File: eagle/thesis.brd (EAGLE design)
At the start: 99.1 x 60.2 mm, 14 parts

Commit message: routed thesis board
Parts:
- moved U$4 46.0 mm to (28.3, 51.9), turned to 180 degrees
- moved U$2 11.0 mm to (22.1, 1.65), turned to 90 degrees
- moved U$3 0.89 mm to (-2.67, 14.7)
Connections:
- new net D52: U$1.52
- new net D53: U$1.53
- net ACCELCS: now also U$1.8; no longer U$1.53
- net GND: no longer U$1.GND_DEBUG
- net RX3H: now also U$2.P$11
- net SDCS: now also U$1.9; no longer U$1.52
- net TX3H: no longer U$2.P$11
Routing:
- net MOSI: track 0.00 -> 189.0 mm, vias 0 -> 6
- net SCLK: track 0.00 -> 124.6 mm, vias 0 -> 5
- net RX3H: track 0.00 -> 96.6 mm
- net 3V3: track 107.0 -> 197.4 mm
- net MISO: track 0.00 -> 73.8 mm, vias 0 -> 4
- net GND: track 244.3 -> 280.4 mm, vias 0 -> 1
- net SDCS: track 0.00 -> 34.4 mm, vias 0 -> 3
- net RX3: track 83.4 -> 105.2 mm, vias 2 -> 0
- net TX3H: track 77.4 -> 97.8 mm
- net ACCELCS: track 0.00 -> 15.2 mm
- net 5V: track 132.2 -> 146.2 mm, vias 0 -> 1
- net TX3: track 73.7 -> 86.5 mm
- net TX2H: track 35.5 -> 25.7 mm
- net SDA2: track 82.6 -> 88.6 mm
- net RX2: track 97.2 -> 102.6 mm
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
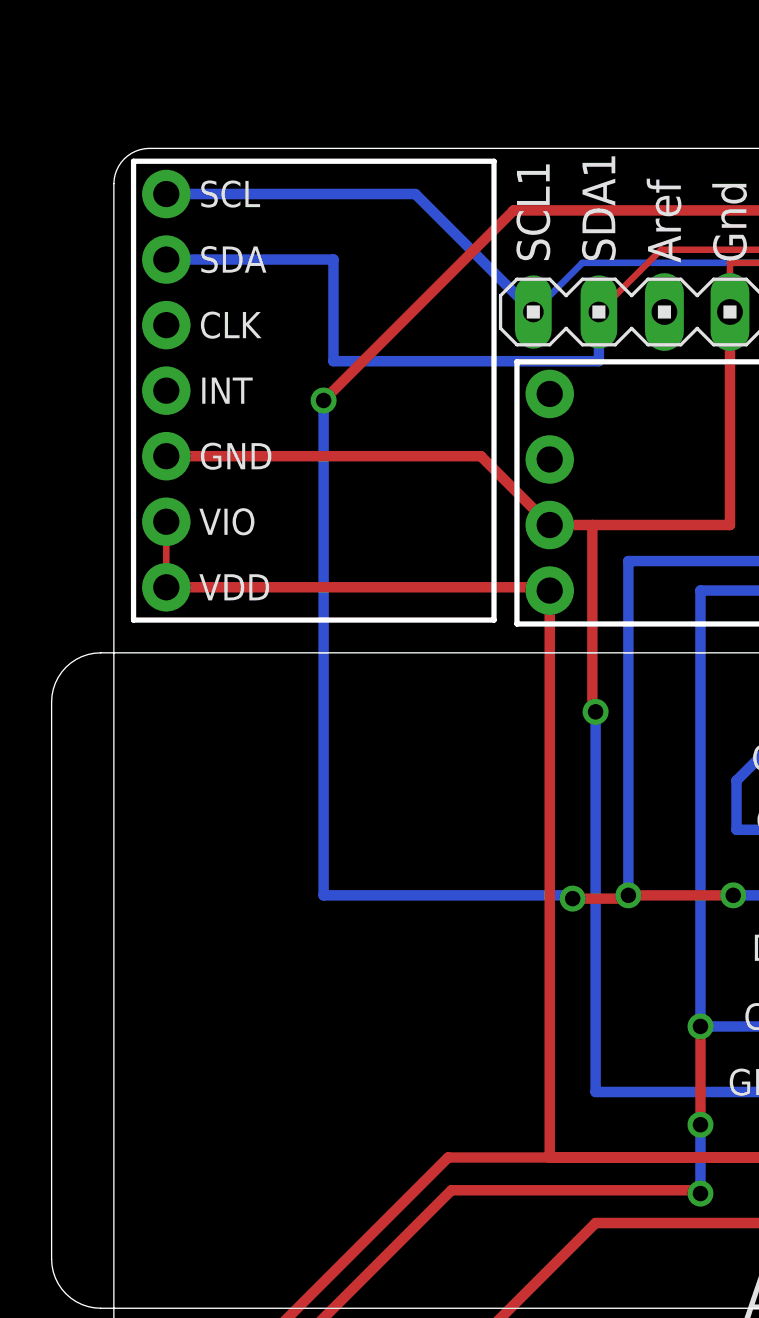
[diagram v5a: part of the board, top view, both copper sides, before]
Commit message: flipped itg3200 board
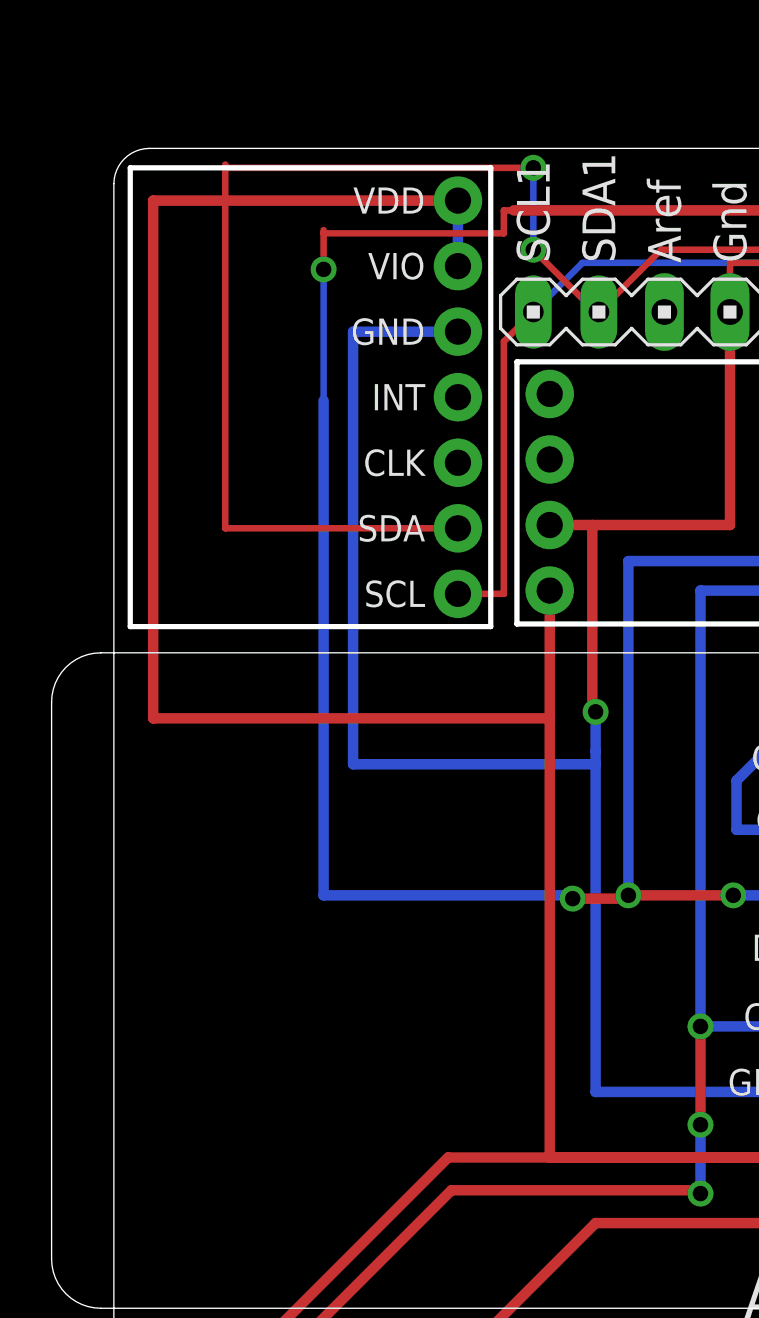
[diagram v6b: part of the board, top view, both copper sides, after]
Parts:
- moved U$7 22.5 mm to (0.64, 59.4), turned to 270 degrees
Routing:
- net 3V3: track 197.4 -> 229.8 mm
- net SDA2: track 88.6 -> 107.8 mm, vias 0 -> 2
- net GND: track 280.4 -> 294.7 mm
- net MOSI: track 189.0 -> 193.4 mm
- net SCL: track 85.0 -> 82.1 mm
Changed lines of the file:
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@@
 <element name="U$2" library="SparkFun-Boards" package="LOGIC_LEVEL_CONVERTER" value="LOGIC_LEVEL_CONVERTER" x="22.098" y="1.651" rot="R90"/>
 <element name="U$4" library="adxl362" package="ADXL362" value="ADXL362" x="28.321" y="51.943" rot="R180"/>
-<element name="U$7" library="ITG3200" package="ITG3200" value="ITG3200" x="14.732" y="41.91" rot="R90"/>
+<element name="U$7" library="ITG3200" package="ITG3200" value="ITG3200" x="0.635" y="59.436" rot="R270"/>
 <element name="U$3" library="MICROSD" package="MICROSD" value="MICROSD" x="-2.667" y="14.732"/>
 <element name="X1" library="con-subd" package="F09V" value="" x="81.407" y="36.449" rot="R90">
@@
 <contactref element="U$4" pad="VCC"/>
 <contactref element="U$2" pad="P$3"/>
-<wire x1="2.032" y1="45.72" x2="2.032" y2="43.18" width="0.254" layer="1"/>
 <wire x1="87.503" y1="9.398" x2="84.455" y2="9.398" width="0.254" layer="1"/>
 <wire x1="87.503" y1="3.683" x2="87.503" y2="9.398" width="0.254" layer="1"/>
@@
 <wire x1="34.671" y1="7.493" x2="43.434" y2="7.493" width="0.254" layer="16"/>
 <wire x1="32.766" y1="5.588" x2="34.671" y2="7.493" width="0.254" layer="16"/>
-<wire x1="2.032" y1="43.18" x2="16.891" y2="43.18" width="0.4064" layer="1"/>
-<wire x1="16.891" y1="43.18" x2="16.891" y2="43.053" width="0.4064" layer="1"/>
-<wire x1="16.891" y1="43.053" x2="16.891" y2="21.082" width="0.4064" layer="1"/>
+<wire x1="16.891" y1="43.053" x2="16.891" y2="38.1" width="0.4064" layer="1"/>
+<wire x1="16.891" y1="38.1" x2="16.891" y2="21.082" width="0.4064" layer="1"/>
 <wire x1="2.794" y1="10.922" x2="2.794" y2="0.889" width="0.4064" layer="1"/>
 <via x="2.794" y="0.889" extent="1-16" drill="0.6"/>
@@
 <wire x1="27.813" y1="21.082" x2="12.954" y2="21.082" width="0.4064" layer="1"/>
 <wire x1="12.954" y1="21.082" x2="2.794" y2="10.922" width="0.4064" layer="1"/>
+<wire x1="13.335" y1="55.626" x2="13.335" y2="58.166" width="0.4064" layer="16"/>
+<wire x1="16.891" y1="43.18" x2="16.891" y2="43.053" width="0.4064" layer="1"/>
+<wire x1="16.891" y1="38.1" x2="1.524" y2="38.1" width="0.4064" layer="1"/>
+<wire x1="1.524" y1="38.1" x2="1.524" y2="58.166" width="0.4064" layer="1"/>
+<wire x1="1.524" y1="58.166" x2="13.335" y2="58.166" width="0.4064" layer="1"/>
 </signal>
 <signal name="5V">
@@
 <wire x1="86.741" y1="50.038" x2="86.741" y2="57.785" width="0.4064" layer="1"/>
 <wire x1="86.741" y1="57.785" x2="15.494" y2="57.785" width="0.4064" layer="1"/>
-<wire x1="15.494" y1="57.785" x2="8.128" y2="50.419" width="0.4064" layer="1"/>
-<via x="8.128" y="50.419" extent="1-16" drill="0.6"/>
 <wire x1="8.128" y1="50.419" x2="8.128" y2="31.242" width="0.4064" layer="16"/>
 <wire x1="8.128" y1="31.242" x2="17.78" y2="31.242" width="0.4064" layer="16"/>
@@
 <wire x1="17.78" y1="31.115" x2="19.939" y2="31.115" width="0.4064" layer="1"/>
 <wire x1="19.939" y1="31.115" x2="19.939" y2="31.242" width="0.4064" layer="1"/>
+<wire x1="15.494" y1="57.785" x2="15.113" y2="57.785" width="0.254" layer="1"/>
+<wire x1="15.113" y1="57.785" x2="15.113" y2="56.896" width="0.254" layer="1"/>
+<wire x1="15.113" y1="56.896" x2="8.128" y2="56.896" width="0.254" layer="1"/>
+<wire x1="8.128" y1="56.896" x2="8.128" y2="57.023" width="0.254" layer="1"/>
+<wire x1="8.128" y1="50.419" x2="8.128" y2="55.499" width="0.254" layer="16"/>
+<via x="8.128" y="55.499" extent="1-16" drill="0.6"/>
+<wire x1="8.128" y1="55.499" x2="8.128" y2="56.896" width="0.254" layer="1"/>
 </signal>
 <signal name="RX2">
@@
 <wire x1="81.661" y1="55.753" x2="18.161" y2="55.753" width="0.254" layer="16"/>
 <wire x1="83.566" y1="53.848" x2="81.661" y2="55.753" width="0.254" layer="16"/>
-<wire x1="2.032" y1="58.42" x2="11.684" y2="58.42" width="0.4064" layer="16"/>
-<wire x1="11.684" y1="58.42" x2="16.256" y2="53.848" width="0.4064" layer="16"/>
+<wire x1="13.335" y1="42.926" x2="15.113" y2="42.926" width="0.254" layer="1"/>
+<wire x1="15.113" y1="42.926" x2="15.113" y2="52.705" width="0.254" layer="1"/>
+<wire x1="15.113" y1="52.705" x2="16.256" y2="53.848" width="0.254" layer="1"/>
 </signal>
 <signal name="SCLK">
@@
 <wire x1="33.909" y1="33.02" x2="33.909" y2="3.683" width="0.254" layer="1"/>
 <wire x1="32.639" y1="34.29" x2="33.909" y2="33.02" width="0.254" layer="1"/>
-<wire x1="2.032" y1="48.26" x2="14.224" y2="48.26" width="0.4064" layer="1"/>
-<wire x1="14.224" y1="48.26" x2="16.891" y2="45.593" width="0.4064" layer="1"/>
 <wire x1="16.891" y1="45.593" x2="18.542" y2="45.593" width="0.4064" layer="1"/>
 <wire x1="18.542" y1="45.593" x2="23.876" y2="45.593" width="0.4064" layer="1"/>
 <wire x1="23.876" y1="45.593" x2="23.876" y2="53.848" width="0.4064" layer="1"/>
 <wire x1="27.813" y1="23.622" x2="18.669" y2="23.622" width="0.4064" layer="16"/>
-<wire x1="18.669" y1="23.622" x2="18.669" y2="38.354" width="0.4064" layer="16"/>
+<wire x1="18.669" y1="23.622" x2="18.669" y2="36.322" width="0.4064" layer="16"/>
 <via x="18.669" y="38.354" extent="1-16" drill="0.6"/>
+<wire x1="18.669" y1="36.83" x2="18.669" y2="38.354" width="0.4064" layer="16"/>
 <wire x1="18.669" y1="38.354" x2="18.542" y2="38.354" width="0.4064" layer="1"/>
 <wire x1="18.542" y1="38.354" x2="18.542" y2="45.593" width="0.4064" layer="1"/>
+<wire x1="13.335" y1="53.086" x2="9.271" y2="53.086" width="0.4064" layer="16"/>
+<wire x1="9.271" y1="53.086" x2="9.271" y2="36.322" width="0.4064" layer="16"/>
+<wire x1="9.271" y1="36.322" x2="18.669" y2="36.322" width="0.4064" layer="16"/>
+<wire x1="18.669" y1="36.322" x2="18.669" y2="36.83" width="0.4064" layer="16"/>
 </signal>
 <signal name="V-">
@@
 <wire x1="18.796" y1="53.848" x2="19.05" y2="53.848" width="0.4064" layer="1"/>
 <wire x1="18.796" y1="53.848" x2="18.669" y2="53.848" width="0.4064" layer="16"/>
-<wire x1="2.032" y1="55.88" x2="8.509" y2="55.88" width="0.4064" layer="16"/>
-<wire x1="8.509" y1="55.88" x2="8.509" y2="51.943" width="0.4064" layer="16"/>
-<wire x1="8.509" y1="51.943" x2="18.796" y2="51.943" width="0.4064" layer="16"/>
-<wire x1="18.796" y1="51.943" x2="18.796" y2="53.848" width="0.4064" layer="16"/>
+<wire x1="13.335" y1="45.466" x2="4.318" y2="45.466" width="0.254" layer="1"/>
+<wire x1="4.318" y1="45.466" x2="4.318" y2="59.436" width="0.254" layer="1"/>
+<wire x1="18.796" y1="53.848" x2="18.669" y2="53.848" width="0.254" layer="1"/>
+<wire x1="18.669" y1="53.848" x2="16.256" y2="56.261" width="0.254" layer="1"/>
+<via x="16.256" y="56.261" extent="1-16" drill="0.6"/>
+<wire x1="16.256" y1="56.261" x2="16.256" y2="59.436" width="0.254" layer="16"/>
+<via x="16.256" y="59.436" extent="1-16" drill="0.6"/>
+<wire x1="16.256" y1="59.436" x2="4.318" y2="59.436" width="0.254" layer="1"/>
+<wire x1="4.318" y1="59.436" x2="4.318" y2="59.563" width="0.254" layer="1"/>
 </signal>
 <signal name="RX3H">

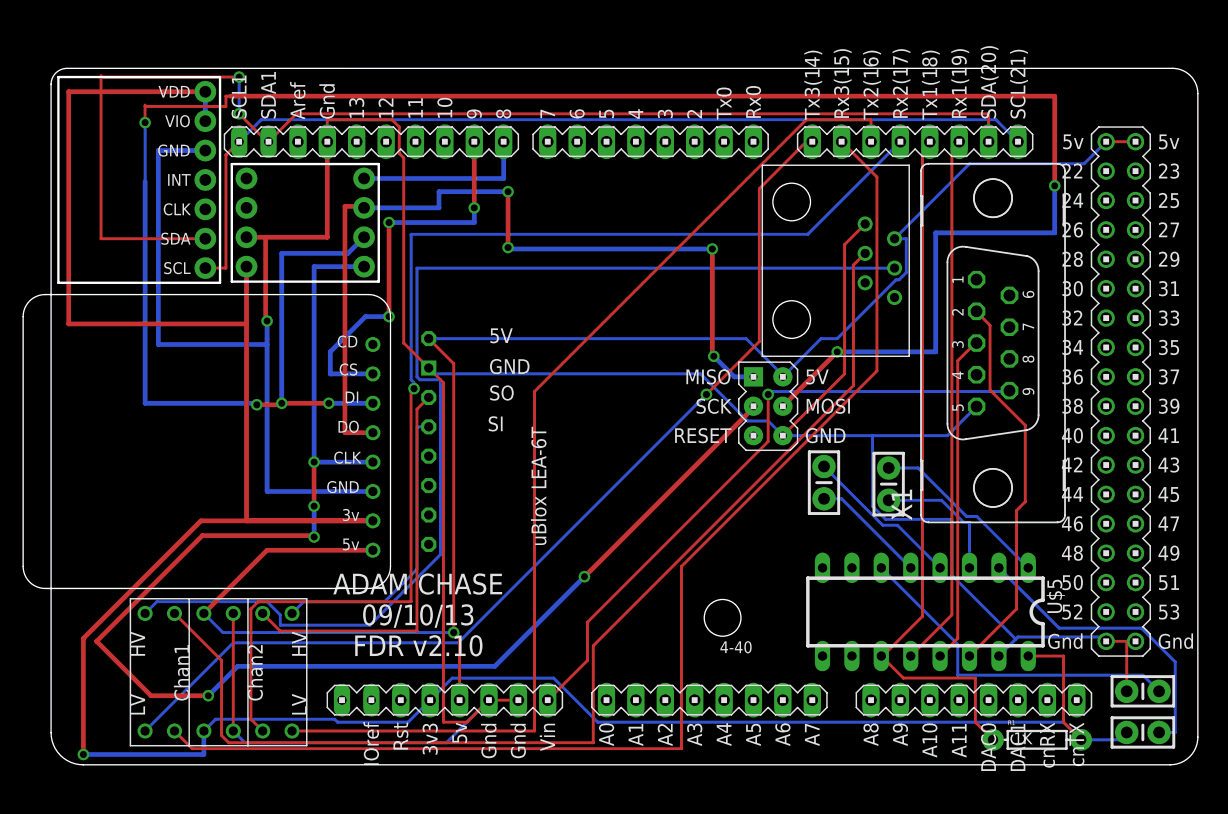
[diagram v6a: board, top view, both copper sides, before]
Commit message: modified eagle files, should be ready to order
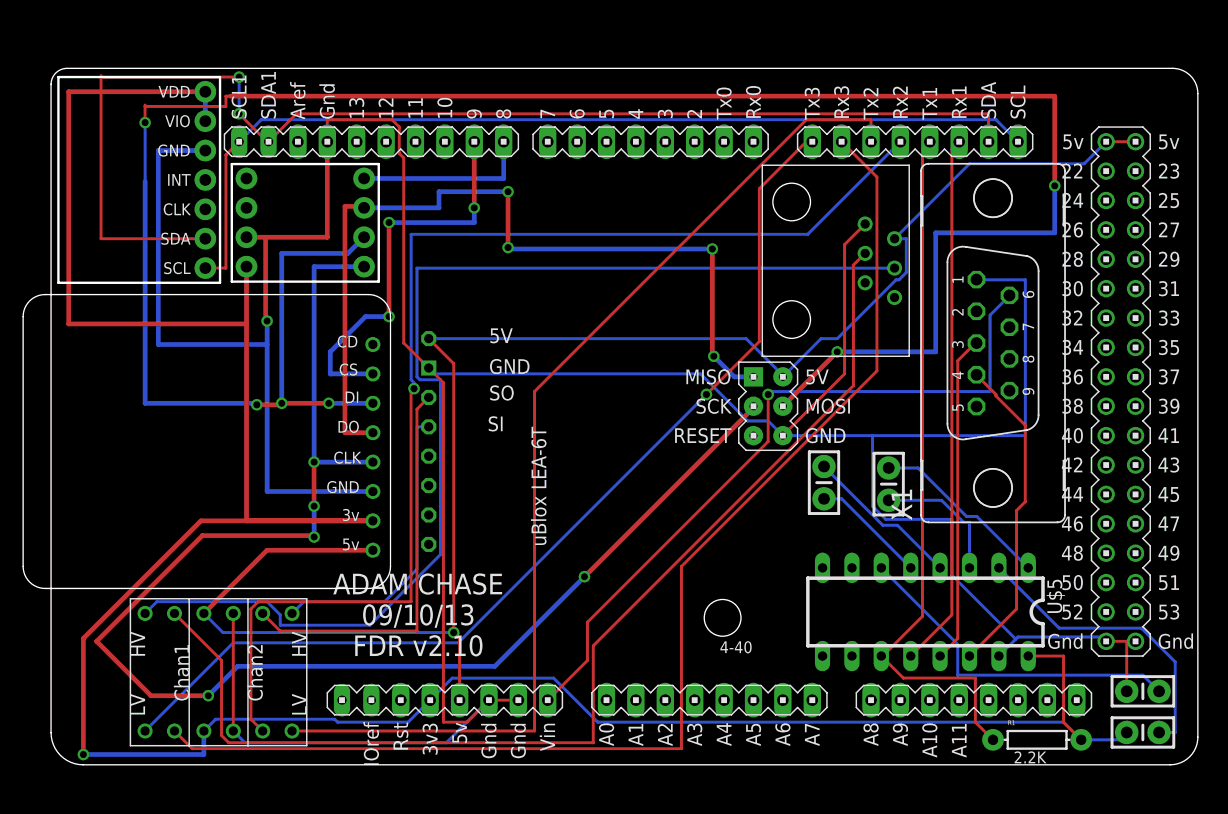
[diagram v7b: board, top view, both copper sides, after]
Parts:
- R1: value 1K -> 2.2K
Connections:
- net GND: now also X1.1; no longer X1.5
- net RS232SO: now also X1.4; no longer X1.2
- net VIN: now also X1.6; no longer X1.9
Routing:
- net GND: track 294.7 -> 315.5 mm
- net VIN: track 55.3 -> 62.6 mm
- net RS232SO: track 33.5 -> 28.0 mm
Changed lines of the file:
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@@
 <text x="37.719" y="28.829" size="1.27" layer="21">SI</text>
 <text x="57.785" y="9.652" size="1.016" layer="21">4-40</text>
-<text x="51.5874" y="40.5638" size="2.794" layer="22" font="vector" rot="MR180" align="center">CAL POLY
+<text x="48.2854" y="39.8018" size="2.794" layer="22" font="vector" rot="MR180" align="center">CAL POLY
 FLIGHT LAB</text>
 <rectangle x1="48.5775" y1="9.4615" x2="48.9585" y2="9.5885" layer="22"/>
@@
 <element name="C3" library="SparkFun-Passives" package="CAP-PTH-SMALL-KIT" value="100nF" x="94.361" y="6.35" rot="R180"/>
 <element name="C4" library="SparkFun-Passives" package="CAP-PTH-SMALL-KIT" value="100nF" x="94.361" y="2.794"/>
-<element name="R1" library="SparkFun-Resistors" package="AXIAL-0.3" value="1K" x="85.217" y="2.159"/>
+<element name="R1" library="SparkFun-Resistors" package="AXIAL-0.3" value="2.2K" x="85.217" y="2.159" smashed="yes">
+<attribute name="NAME" x="82.677" y="3.429" size="0.4064" layer="25" font="vector"/>
+<attribute name="VALUE" x="83.185" y="0.127" size="1.016" layer="21" font="vector" ratio="15"/>
+</element>
 <element name="U$8" library="RJ11V" package="RJ11V" value="RJ11V" x="74.168" y="35.306" rot="R90"/>
 </elements>
@@
 <signal name="VIN">
 <contactref element="U$1" pad="VIN"/>
-<contactref element="X1" pad="9"/>
 <wire x1="46.355" y1="9.017" x2="42.926" y2="5.588" width="0.254" layer="1"/>
 <wire x1="46.355" y1="12.319" x2="46.355" y2="9.017" width="0.254" layer="1"/>
 <wire x1="61.976" y1="27.94" x2="46.355" y2="12.319" width="0.254" layer="1"/>
 <wire x1="61.976" y1="32.004" x2="61.976" y2="27.94" width="0.254" layer="1"/>
+<via x="61.976" y="32.004" extent="1-16" drill="0.6096"/>
+<contactref element="X1" pad="6"/>
+<wire x1="81.153" y1="38.862" x2="82.804" y2="40.513" width="0.254" layer="16"/>
+<wire x1="81.153" y1="32.258" x2="81.153" y2="38.862" width="0.254" layer="16"/>
+<wire x1="62.23" y1="32.258" x2="81.153" y2="32.258" width="0.254" layer="16"/>
+<wire x1="82.804" y1="40.513" x2="82.8294" y2="40.5638" width="0.254" layer="16"/>
 <wire x1="62.23" y1="32.258" x2="61.976" y2="32.004" width="0.254" layer="16"/>
-<wire x1="82.804" y1="32.258" x2="62.23" y2="32.258" width="0.254" layer="16"/>
-<wire x1="82.804" y1="32.258" x2="82.8294" y2="32.3342" width="0.254" layer="16"/>
-<via x="61.976" y="32.004" extent="1-16" drill="0.6096"/>
 </signal>
 <signal name="SCL">
@@
 <contactref element="U$5" pad="15"/>
 <contactref element="C3" pad="2"/>
-<contactref element="X1" pad="5"/>
 <contactref element="U$3" pad="GND"/>
 <contactref element="U$7" pad="GND"/>
@@
 <wire x1="68.58" y1="33.782" x2="68.58" y2="44.958" width="0.254" layer="1"/>
 <wire x1="63.246" y1="28.448" x2="68.58" y2="33.782" width="0.254" layer="1"/>
-<wire x1="77.47" y1="28.448" x2="79.9846" y2="30.9626" width="0.254" layer="16"/>
 <wire x1="63.246" y1="28.448" x2="70.993" y2="28.448" width="0.254" layer="16"/>
-<wire x1="70.993" y1="28.448" x2="77.47" y2="28.448" width="0.254" layer="16"/>
 <wire x1="77.851" y1="16.383" x2="83.3755" y2="10.8585" width="0.254" layer="16"/>
 <wire x1="77.851" y1="21.209" x2="77.851" y2="16.383" width="0.254" layer="16"/>
@@
 <wire x1="18.669" y1="23.622" x2="18.669" y2="36.322" width="0.4064" layer="16"/>
 <via x="18.669" y="38.354" extent="1-16" drill="0.6"/>
-<wire x1="18.669" y1="36.83" x2="18.669" y2="38.354" width="0.4064" layer="16"/>
+<wire x1="18.669" y1="36.322" x2="18.669" y2="38.354" width="0.4064" layer="16"/>
 <wire x1="18.669" y1="38.354" x2="18.542" y2="38.354" width="0.4064" layer="1"/>
 <wire x1="18.542" y1="38.354" x2="18.542" y2="45.593" width="0.4064" layer="1"/>
@@
 <wire x1="9.271" y1="53.086" x2="9.271" y2="36.322" width="0.4064" layer="16"/>
 <wire x1="9.271" y1="36.322" x2="18.669" y2="36.322" width="0.4064" layer="16"/>
-<wire x1="18.669" y1="36.322" x2="18.669" y2="36.83" width="0.4064" layer="16"/>
+<contactref element="X1" pad="1"/>
+<wire x1="70.993" y1="28.448" x2="84.201" y2="28.448" width="0.254" layer="16"/>
+<wire x1="80.391" y1="41.91" x2="79.9846" y2="41.9354" width="0.254" layer="16"/>
+<wire x1="84.201" y1="41.91" x2="80.391" y2="41.91" width="0.254" layer="16"/>
+<wire x1="84.201" y1="28.448" x2="84.201" y2="41.91" width="0.254" layer="16"/>
 </signal>
 <signal name="V-">
@@
 <signal name="RS232SO">
 <contactref element="U$5" pad="14"/>
-<contactref element="X1" pad="2"/>
 <wire x1="83.439" y1="13.462" x2="79.375" y2="9.398" width="0.254" layer="1"/>
 <wire x1="83.439" y1="21.971" x2="83.439" y2="13.462" width="0.254" layer="1"/>
 <wire x1="84.201" y1="22.733" x2="83.439" y2="21.971" width="0.254" layer="1"/>
 <wire x1="84.201" y1="29.337" x2="84.201" y2="22.733" width="0.254" layer="1"/>
-<wire x1="81.153" y1="32.385" x2="84.201" y2="29.337" width="0.254" layer="1"/>
-<wire x1="81.153" y1="37.973" x2="81.153" y2="32.385" width="0.254" layer="1"/>
-<wire x1="80.01" y1="39.116" x2="81.153" y2="37.973" width="0.254" layer="1"/>
-<wire x1="80.01" y1="39.116" x2="79.9846" y2="39.1922" width="0.254" layer="1"/>
+<contactref element="X1" pad="4"/>
+<wire x1="81.661" y1="32.004" x2="80.01" y2="33.655" width="0.254" layer="1"/>
+<wire x1="81.661" y1="31.877" x2="81.661" y2="32.004" width="0.254" layer="1"/>
+<wire x1="84.201" y1="29.337" x2="81.661" y2="31.877" width="0.254" layer="1"/>
+<wire x1="80.01" y1="33.655" x2="79.9846" y2="33.7058" width="0.254" layer="1"/>
 </signal>
 <signal name="RS232SI">
 <contactref element="U$5" pad="13"/>
+<wire x1="78.359" y1="10.922" x2="76.835" y2="9.398" width="0.254" layer="1"/>
 <contactref element="X1" pad="3"/>
-<wire x1="78.359" y1="10.922" x2="76.835" y2="9.398" width="0.254" layer="1"/>
 <wire x1="78.359" y1="34.925" x2="78.359" y2="10.922" width="0.254" layer="1"/>
 <wire x1="79.883" y1="36.449" x2="78.359" y2="34.925" width="0.254" layer="1"/>

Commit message: modified eagle boards, ordered them.
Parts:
- renumbered U$5 to MAX3232
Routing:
- net SDA2: track 107.8 -> 84.4 mm, vias 2 -> 0
- net 3V3: track 229.8 -> 221.7 mm, vias 1 -> 0
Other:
- board text added: "100nF"
- board text added: "ADAM CHASE 10/22/13 FDR v3.00BOB"
- board text removed: "ADAM CHASE 09/10/13 FDR v2.10"
